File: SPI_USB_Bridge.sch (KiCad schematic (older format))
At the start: 31 parts, among them J6 USB A RECEP., Q5 IRLML2502, Q6 IRLML2502, U15 CY7C65634-28LTXC, U9 MAX3421, Y2 12MHz, Y3 12MHz

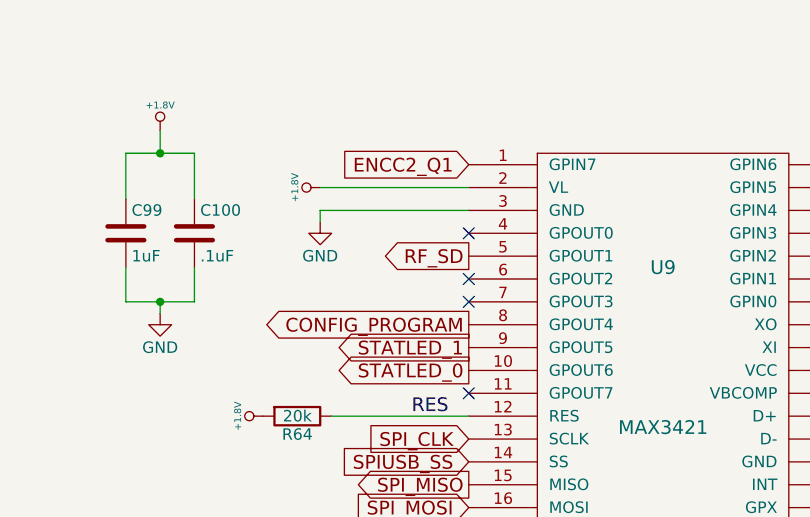
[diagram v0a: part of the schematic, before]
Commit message: encoders and headphone jack have been modified. many unconnections
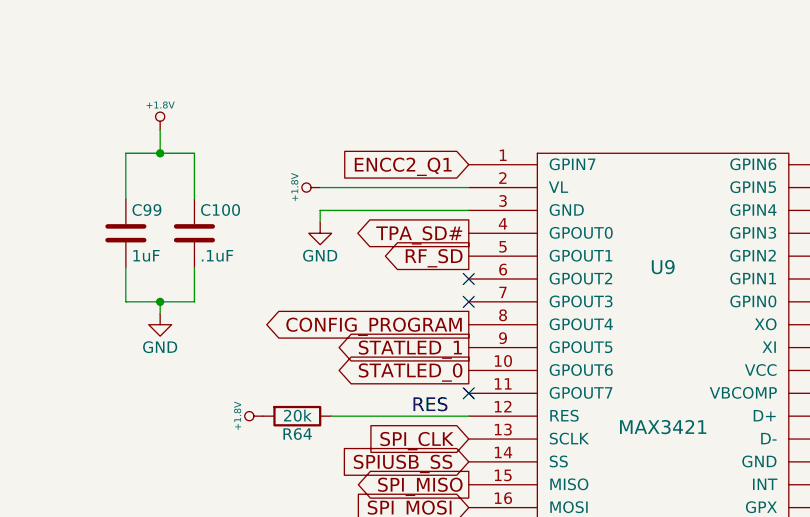
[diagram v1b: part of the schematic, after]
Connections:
- net labels added: TPA_SD#
- no-connect marks 7 -> 6
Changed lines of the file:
@@
 LIBS:DFTCustom
 LIBS:TLV320AIC3104
+LIBS:tpa2010d1
+LIBS:lis2hh12
+LIBS:Ghost
+LIBS:asflmb
+LIBS:er-con06hb-1
+LIBS:jack_trs_4pins
 EELAYER 25 0
 EELAYER END
@@
 $EndComp
 $Comp
-L +1.8V #PWR0168
+L +1.8V #PWR0169
 U 1 1 5862C5D3
 P 1850 1550
-F 0 "#PWR0168" H 1850 1690 20  0001 C CNN
+F 0 "#PWR0169" H 1850 1690 20  0001 C CNN
 F 1 "+1.8V" H 1850 1660 30  0000 C CNN
 F 2 "" H 1850 1550 60  0001 C CNN
@@
 $EndComp
 $Comp
-L GND #PWR0169
+L GND #PWR0170
 U 1 1 5862C61D
 P 1850 2350
-F 0 "#PWR0169" H 1850 2100 50  0001 C CNN
+F 0 "#PWR0170" H 1850 2100 50  0001 C CNN
 F 1 "GND" H 1850 2200 50  0000 C CNN
 F 2 "" H 1850 2350 50  0000 C CNN
@@
 $EndComp
 $Comp
-L GND #PWR0170
+L GND #PWR0171
 U 1 1 5862C682
 P 5650 3350
-F 0 "#PWR0170" H 5650 3100 50  0001 C CNN
+F 0 "#PWR0171" H 5650 3100 50  0001 C CNN
 F 1 "GND" H 5650 3200 50  0000 C CNN
 F 2 "" H 5650 3350 50  0000 C CNN
@@
 SPIUSB_GPX
 $Comp
-L GND #PWR0171
+L GND #PWR0172
 U 1 1 5862D1A5
 P 9050 4750
-F 0 "#PWR0171" H 9050 4500 50  0001 C CNN
+F 0 "#PWR0172" H 9050 4500 50  0001 C CNN
 F 1 "GND" H 9050 4600 50  0000 C CNN
 F 2 "" H 9050 4750 50  0000 C CNN
@@
 $EndComp
 $Comp
-L GND #PWR0172
+L GND #PWR0173
 U 1 1 5862D52A
 P 6750 3200
-F 0 "#PWR0172" H 6750 2950 50  0001 C CNN
+F 0 "#PWR0173" H 6750 2950 50  0001 C CNN
 F 1 "GND" H 6750 3050 50  0000 C CNN
 F 2 "" H 6750 3200 50  0000 C CNN
@@
 $EndComp
 $Comp
-L GND #PWR0173
+L GND #PWR0174
 U 1 1 5862DAA7
 P 6250 1950
-F 0 "#PWR0173" H 6250 1700 50  0001 C CNN
+F 0 "#PWR0174" H 6250 1700 50  0001 C CNN
 F 1 "GND" H 6250 1800 50  0000 C CNN
 F 2 "" H 6250 1950 50  0000 C CNN
@@
 $EndComp
 $Comp
-L +5V #PWR0174
+L +5V #PWR0175
 U 1 1 5862DFFF
 P 7900 1250
-F 0 "#PWR0174" H 7900 1100 50  0001 C CNN
+F 0 "#PWR0175" H 7900 1100 50  0001 C CNN
 F 1 "+5V" H 7900 1390 50  0000 C CNN
 F 2 "" H 7900 1250 50  0000 C CNN
@@
 $EndComp
 $Comp
-L GND #PWR0175
+L GND #PWR0176
 U 1 1 5862E157
 P 8000 1800
-F 0 "#PWR0175" H 8000 1550 50  0001 C CNN
+F 0 "#PWR0176" H 8000 1550 50  0001 C CNN
 F 1 "GND" H 8000 1650 50  0000 C CNN
 F 2 "" H 8000 1800 50  0000 C CNN
@@
 	9200 1650 9200 1750
 $Comp
-L +5V #PWR0176
+L +5V #PWR0177
 U 1 1 5862E815
 P 9200 2150
-F 0 "#PWR0176" H 9200 2000 50  0001 C CNN
+F 0 "#PWR0177" H 9200 2000 50  0001 C CNN
 F 1 "+5V" H 9200 2290 50  0000 C CNN
 F 2 "" H 9200 2150 50  0000 C CNN
@@
 $EndComp
 $Comp
-L GND #PWR0177
+L GND #PWR0178
 U 1 1 586FEB40
 P 2050 7300
-F 0 "#PWR0177" H 2050 7050 50  0001 C CNN
+F 0 "#PWR0178" H 2050 7050 50  0001 C CNN
 F 1 "GND" H 2050 7150 50  0000 C CNN
 F 2 "" H 2050 7300 50  0000 C CNN
@@
 $EndComp
 $Comp
-L GND #PWR0178
+L GND #PWR0179
 U 1 1 586FEDFD
 P 2050 5500
-F 0 "#PWR0178" H 2050 5250 50  0001 C CNN
+F 0 "#PWR0179" H 2050 5250 50  0001 C CNN
 F 1 "GND" H 2050 5350 50  0000 C CNN
 F 2 "" H 2050 5500 50  0000 C CNN
@@
 	2050 6350 2050 6250
 $Comp
-L +5V #PWR0179
+L +5V #PWR0180
 U 1 1 58700335
 P 2050 5950
-F 0 "#PWR0179" H 2050 5800 50  0001 C CNN
+F 0 "#PWR0180" H 2050 5800 50  0001 C CNN
 F 1 "+5V" H 2050 6090 50  0000 C CNN
 F 2 "" H 2050 5950 50  0000 C CNN
@@
 	2050 5950 2050 6050
 $Comp
-L +5V #PWR0180
+L +5V #PWR0181
 U 1 1 58700402
 P 2050 4200
-F 0 "#PWR0180" H 2050 4050 50  0001 C CNN
+F 0 "#PWR0181" H 2050 4050 50  0001 C CNN
 F 1 "+5V" H 2050 4340 50  0000 C CNN
 F 2 "" H 2050 4200 50  0000 C CNN
@@
 	9050 4600 9900 4600
 $Comp
-L +3.3V #PWR0181
+L +3.3V #PWR0182
 U 1 1 58742C2F
 P 6950 2600
-F 0 "#PWR0181" H 6950 2450 50  0001 C CNN
+F 0 "#PWR0182" H 6950 2450 50  0001 C CNN
 F 1 "+3.3V" H 6950 2740 50  0000 C CNN
 F 2 "" H 6950 2600 50  0000 C CNN
@@
 	3200 2800 2600 2800
 $Comp
-L +1.8V #PWR0182
+L +1.8V #PWR0183
 U 1 1 58830992
 P 2300 2800
-F 0 "#PWR0182" H 2300 2940 20  0001 C CNN
+F 0 "#PWR0183" H 2300 2940 20  0001 C CNN
 F 1 "+1.8V" H 2300 2910 30  0000 C CNN
 F 2 "" H 2300 2800 60  0001 C CNN
@@
 $EndComp
 $Comp
-L GND #PWR0183
+L GND #PWR0184
 U 1 1 58830D05
 P 2550 1950
-F 0 "#PWR0183" H 2550 1700 50  0001 C CNN
+F 0 "#PWR0184" H 2550 1700 50  0001 C CNN
 F 1 "GND" H 2550 1800 50  0000 C CNN
 F 2 "" H 2550 1950 50  0000 C CNN
@@
 	1700 1650 2000 1650
 $Comp
-L +1.8V #PWR0184
+L +1.8V #PWR0185
 U 1 1 58830E48
 P 2550 1800
-F 0 "#PWR0184" H 2550 1940 20  0001 C CNN
+F 0 "#PWR0185" H 2550 1940 20  0001 C CNN
 F 1 "+1.8V" H 2550 1910 30  0000 C CNN
 F 2 "" H 2550 1800 60  0001 C CNN
@@
 $EndComp
 $Comp
-L GND #PWR0185
+L GND #PWR0186
 U 1 1 5883B9EA
 P 9750 5150
-F 0 "#PWR0185" H 9750 4900 50  0001 C CNN
+F 0 "#PWR0186" H 9750 4900 50  0001 C CNN
 F 1 "GND" H 9750 5000 50  0000 C CNN
 F 2 "" H 9750 5150 50  0000 C CNN
@@
 SPIUSB2_D_N
 $Comp
-L GND #PWR0186
+L GND #PWR0187
 U 1 1 5883DB26
 P 7200 6300
-F 0 "#PWR0186" H 7200 6050 50  0001 C CNN
+F 0 "#PWR0187" H 7200 6050 50  0001 C CNN
 F 1 "GND" H 7200 6150 50  0000 C CNN
 F 2 "" H 7200 6300 50  0000 C CNN
@@
 Connection ~ 9200 1650
 $Comp
-L +5V #PWR0187
+L +5V #PWR0188
 U 1 1 5883FEC9
 P 7900 2650
-F 0 "#PWR0187" H 7900 2500 50  0001 C CNN
+F 0 "#PWR0188" H 7900 2500 50  0001 C CNN
 F 1 "+5V" H 7900 2790 50  0000 C CNN
 F 2 "" H 7900 2650 50  0000 C CNN
@@
 $EndComp
 $Comp
-L GND #PWR0188
+L GND #PWR0189
 U 1 1 5883FED5
 P 8000 3200
-F 0 "#PWR0188" H 8000 2950 50  0001 C CNN
+F 0 "#PWR0189" H 8000 2950 50  0001 C CNN
 F 1 "GND" H 8000 3050 50  0000 C CNN
 F 2 "" H 8000 3200 50  0000 C CNN
@@
 	9200 3050 9200 3150
 $Comp
-L +5V #PWR0189
+L +5V #PWR0190
 U 1 1 5883FEE8
 P 9200 3550
-F 0 "#PWR0189" H 9200 3400 50  0001 C CNN
+F 0 "#PWR0190" H 9200 3400 50  0001 C CNN
 F 1 "+5V" H 9200 3690 50  0000 C CNN
 F 2 "" H 9200 3550 50  0000 C CNN
@@
 SPIUSB_FAULT1
 $Comp
-L +3.3V #PWR0190
+L +3.3V #PWR0191
 U 1 1 588455D9
 P 5650 4350
-F 0 "#PWR0190" H 5650 4200 50  0001 C CNN
+F 0 "#PWR0191" H 5650 4200 50  0001 C CNN
 F 1 "+3.3V" H 5650 4490 50  0000 C CNN
 F 2 "" H 5650 4350 50  0000 C CNN
@@
 Connection ~ 4500 5350
 $Comp
-L GND #PWR0191
+L GND #PWR0192
 U 1 1 58847DF3
 P 4500 5750
-F 0 "#PWR0191" H 4500 5500 50  0001 C CNN
+F 0 "#PWR0192" H 4500 5500 50  0001 C CNN
 F 1 "GND" H 4500 5600 50  0000 C CNN
 F 2 "" H 4500 5750 50  0000 C CNN
@@
 	4500 5650 4500 5750
 $Comp
-L GND #PWR0192
+L GND #PWR0193
 U 1 1 58847FC6
 P 4500 4750
-F 0 "#PWR0192" H 4500 4500 50  0001 C CNN
+F 0 "#PWR0193" H 4500 4500 50  0001 C CNN
 F 1 "GND" H 4500 4600 50  0000 C CNN
 F 2 "" H 4500 4750 50  0000 C CNN
@@
 	4900 5400 4900 5500
 $Comp
-L +3.3V #PWR0193
+L +3.3V #PWR0194
 U 1 1 5884A193
 P 4900 6000
-F 0 "#PWR0193" H 4900 5850 50  0001 C CNN
+F 0 "#PWR0194" H 4900 5850 50  0001 C CNN
 F 1 "+3.3V" H 4900 6140 50  0000 C CNN
 F 2 "" H 4900 6000 50  0000 C CNN
@@
 	4900 5800 4900 6000
 $Comp
-L +3.3V #PWR0194
+L +3.3V #PWR0195
 U 1 1 5884ACF4
 P 5700 5500
-F 0 "#PWR0194" H 5700 5350 50  0001 C CNN
+F 0 "#PWR0195" H 5700 5350 50  0001 C CNN
 F 1 "+3.3V" H 5700 5640 50  0000 C CNN
 F 2 "" H 5700 5500 50  0000 C CNN
@@
 	5950 5600 5200 5600
 $Comp
-L GND #PWR0195
+L GND #PWR0196
 U 1 1 5884B679
 P 5200 6000
-F 0 "#PWR0195" H 5200 5750 50  0001 C CNN
+F 0 "#PWR0196" H 5200 5750 50  0001 C CNN
 F 1 "GND" H 5200 5850 50  0000 C CNN
 F 2 "" H 5200 6000 50  0000 C CNN
@@
 $EndComp
 $Comp
-L GND #PWR0196
+L GND #PWR0197
 U 1 1 5884BCCD
 P 5450 6000
-F 0 "#PWR0196" H 5450 5750 50  0001 C CNN
+F 0 "#PWR0197" H 5450 5750 50  0001 C CNN
 F 1 "GND" H 5450 5850 50  0000 C CNN
 F 2 "" H 5450 6000 50  0000 C CNN
@@
 	5450 5700 5950 5700
 $Comp
-L GND #PWR0197
+L GND #PWR0198
 U 1 1 5884CAD1
 P 5650 6000
-F 0 "#PWR0197" H 5650 5750 50  0001 C CNN
+F 0 "#PWR0198" H 5650 5750 50  0001 C CNN
 F 1 "GND" H 5650 5850 50  0000 C CNN
 F 2 "" H 5650 6000 50  0000 C CNN
@@
 NoConn ~ 3200 2200
 NoConn ~ 3200 2300
-NoConn ~ 3200 2000
+Text GLabel 3200 2000 0    60   Output ~ 0
+TPA_SD#
 $EndSCHEMATC

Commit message: screen attached!
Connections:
- net labels removed: RF_SD
- no-connect marks 6 -> 7
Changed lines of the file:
@@
 $Descr A4 11693 8268
 encoding utf-8
-Sheet 13 15
+Sheet 13 14
 Title ""
 Date ""
@@
 $EndComp
 $Comp
-L +1.8V #PWR0169
+L +1.8V #PWR0162
 U 1 1 5862C5D3
 P 1850 1550
-F 0 "#PWR0169" H 1850 1690 20  0001 C CNN
+F 0 "#PWR0162" H 1850 1690 20  0001 C CNN
 F 1 "+1.8V" H 1850 1660 30  0000 C CNN
 F 2 "" H 1850 1550 60  0001 C CNN
@@
 $EndComp
 $Comp
-L GND #PWR0170
+L GND #PWR0163
 U 1 1 5862C61D
 P 1850 2350
-F 0 "#PWR0170" H 1850 2100 50  0001 C CNN
+F 0 "#PWR0163" H 1850 2100 50  0001 C CNN
 F 1 "GND" H 1850 2200 50  0000 C CNN
 F 2 "" H 1850 2350 50  0000 C CNN
@@
 $EndComp
 $Comp
-L GND #PWR0171
+L GND #PWR0164
 U 1 1 5862C682
 P 5650 3350
-F 0 "#PWR0171" H 5650 3100 50  0001 C CNN
+F 0 "#PWR0164" H 5650 3100 50  0001 C CNN
 F 1 "GND" H 5650 3200 50  0000 C CNN
 F 2 "" H 5650 3350 50  0000 C CNN
@@
 SPIUSB_GPX
 $Comp
-L GND #PWR0172
+L GND #PWR0165
 U 1 1 5862D1A5
 P 9050 4750
-F 0 "#PWR0172" H 9050 4500 50  0001 C CNN
+F 0 "#PWR0165" H 9050 4500 50  0001 C CNN
 F 1 "GND" H 9050 4600 50  0000 C CNN
 F 2 "" H 9050 4750 50  0000 C CNN
@@
 $EndComp
 $Comp
-L GND #PWR0173
+L GND #PWR0166
 U 1 1 5862D52A
 P 6750 3200
-F 0 "#PWR0173" H 6750 2950 50  0001 C CNN
+F 0 "#PWR0166" H 6750 2950 50  0001 C CNN
 F 1 "GND" H 6750 3050 50  0000 C CNN
 F 2 "" H 6750 3200 50  0000 C CNN
@@
 $EndComp
 $Comp
-L GND #PWR0174
+L GND #PWR0167
 U 1 1 5862DAA7
 P 6250 1950
-F 0 "#PWR0174" H 6250 1700 50  0001 C CNN
+F 0 "#PWR0167" H 6250 1700 50  0001 C CNN
 F 1 "GND" H 6250 1800 50  0000 C CNN
 F 2 "" H 6250 1950 50  0000 C CNN
@@
 $EndComp
 $Comp
-L +5V #PWR0175
+L +5V #PWR0168
 U 1 1 5862DFFF
 P 7900 1250
-F 0 "#PWR0175" H 7900 1100 50  0001 C CNN
+F 0 "#PWR0168" H 7900 1100 50  0001 C CNN
 F 1 "+5V" H 7900 1390 50  0000 C CNN
 F 2 "" H 7900 1250 50  0000 C CNN
@@
 $EndComp
 $Comp
-L GND #PWR0176
+L GND #PWR0169
 U 1 1 5862E157
 P 8000 1800
-F 0 "#PWR0176" H 8000 1550 50  0001 C CNN
+F 0 "#PWR0169" H 8000 1550 50  0001 C CNN
 F 1 "GND" H 8000 1650 50  0000 C CNN
 F 2 "" H 8000 1800 50  0000 C CNN
@@
 	9200 1650 9200 1750
 $Comp
-L +5V #PWR0177
+L +5V #PWR0170
 U 1 1 5862E815
 P 9200 2150
-F 0 "#PWR0177" H 9200 2000 50  0001 C CNN
+F 0 "#PWR0170" H 9200 2000 50  0001 C CNN
 F 1 "+5V" H 9200 2290 50  0000 C CNN
 F 2 "" H 9200 2150 50  0000 C CNN
@@
 Wire Wire Line
 	1700 2300 2000 2300
-Text GLabel 3200 2100 0    60   Output ~ 0
-RF_SD
 Text GLabel 3200 2400 0    60   Output ~ 0
 CONFIG_PROGRAM
@@
 $EndComp
 $Comp
-L GND #PWR0178
+L GND #PWR0171
 U 1 1 586FEB40
 P 2050 7300
-F 0 "#PWR0178" H 2050 7050 50  0001 C CNN
+F 0 "#PWR0171" H 2050 7050 50  0001 C CNN
 F 1 "GND" H 2050 7150 50  0000 C CNN
 F 2 "" H 2050 7300 50  0000 C CNN
@@
 $EndComp
 $Comp
-L GND #PWR0179
+L GND #PWR0172
 U 1 1 586FEDFD
 P 2050 5500
-F 0 "#PWR0179" H 2050 5250 50  0001 C CNN
+F 0 "#PWR0172" H 2050 5250 50  0001 C CNN
 F 1 "GND" H 2050 5350 50  0000 C CNN
 F 2 "" H 2050 5500 50  0000 C CNN
@@
 	2050 6350 2050 6250
 $Comp
-L +5V #PWR0180
+L +5V #PWR0173
 U 1 1 58700335
 P 2050 5950
-F 0 "#PWR0180" H 2050 5800 50  0001 C CNN
+F 0 "#PWR0173" H 2050 5800 50  0001 C CNN
 F 1 "+5V" H 2050 6090 50  0000 C CNN
 F 2 "" H 2050 5950 50  0000 C CNN
@@
 	2050 5950 2050 6050
 $Comp
-L +5V #PWR0181
+L +5V #PWR0174
 U 1 1 58700402
 P 2050 4200
-F 0 "#PWR0181" H 2050 4050 50  0001 C CNN
+F 0 "#PWR0174" H 2050 4050 50  0001 C CNN
 F 1 "+5V" H 2050 4340 50  0000 C CNN
 F 2 "" H 2050 4200 50  0000 C CNN
@@
 	9050 4600 9900 4600
 $Comp
-L +3.3V #PWR0182
+L +3.3V #PWR0175
 U 1 1 58742C2F
 P 6950 2600
-F 0 "#PWR0182" H 6950 2450 50  0001 C CNN
+F 0 "#PWR0175" H 6950 2450 50  0001 C CNN
 F 1 "+3.3V" H 6950 2740 50  0000 C CNN
 F 2 "" H 6950 2600 50  0000 C CNN
@@
 	3200 2800 2600 2800
 $Comp
-L +1.8V #PWR0183
+L +1.8V #PWR0176
 U 1 1 58830992
 P 2300 2800
-F 0 "#PWR0183" H 2300 2940 20  0001 C CNN
+F 0 "#PWR0176" H 2300 2940 20  0001 C CNN
 F 1 "+1.8V" H 2300 2910 30  0000 C CNN
 F 2 "" H 2300 2800 60  0001 C CNN
@@
 $EndComp
 $Comp
-L GND #PWR0184
+L GND #PWR0177
 U 1 1 58830D05
 P 2550 1950
-F 0 "#PWR0184" H 2550 1700 50  0001 C CNN
+F 0 "#PWR0177" H 2550 1700 50  0001 C CNN
 F 1 "GND" H 2550 1800 50  0000 C CNN
 F 2 "" H 2550 1950 50  0000 C CNN
@@
 	1700 1650 2000 1650
 $Comp
-L +1.8V #PWR0185
+L +1.8V #PWR0178
 U 1 1 58830E48
 P 2550 1800
-F 0 "#PWR0185" H 2550 1940 20  0001 C CNN
+F 0 "#PWR0178" H 2550 1940 20  0001 C CNN
 F 1 "+1.8V" H 2550 1910 30  0000 C CNN
 F 2 "" H 2550 1800 60  0001 C CNN
@@
 $EndComp
 $Comp
-L GND #PWR0186
+L GND #PWR0179
 U 1 1 5883B9EA
 P 9750 5150
-F 0 "#PWR0186" H 9750 4900 50  0001 C CNN
+F 0 "#PWR0179" H 9750 4900 50  0001 C CNN
 F 1 "GND" H 9750 5000 50  0000 C CNN
 F 2 "" H 9750 5150 50  0000 C CNN
@@
 SPIUSB2_D_N
 $Comp
-L GND #PWR0187
+L GND #PWR0180
 U 1 1 5883DB26
 P 7200 6300
-F 0 "#PWR0187" H 7200 6050 50  0001 C CNN
+F 0 "#PWR0180" H 7200 6050 50  0001 C CNN
 F 1 "GND" H 7200 6150 50  0000 C CNN
 F 2 "" H 7200 6300 50  0000 C CNN
@@
 Connection ~ 9200 1650
 $Comp
-L +5V #PWR0188
+L +5V #PWR0181
 U 1 1 5883FEC9
 P 7900 2650
-F 0 "#PWR0188" H 7900 2500 50  0001 C CNN
+F 0 "#PWR0181" H 7900 2500 50  0001 C CNN
 F 1 "+5V" H 7900 2790 50  0000 C CNN
 F 2 "" H 7900 2650 50  0000 C CNN
@@
 $EndComp
 $Comp
-L GND #PWR0189
+L GND #PWR0182
 U 1 1 5883FED5
 P 8000 3200
-F 0 "#PWR0189" H 8000 2950 50  0001 C CNN
+F 0 "#PWR0182" H 8000 2950 50  0001 C CNN
 F 1 "GND" H 8000 3050 50  0000 C CNN
 F 2 "" H 8000 3200 50  0000 C CNN
@@
 	9200 3050 9200 3150
 $Comp
-L +5V #PWR0190
+L +5V #PWR0183
 U 1 1 5883FEE8
 P 9200 3550
-F 0 "#PWR0190" H 9200 3400 50  0001 C CNN
+F 0 "#PWR0183" H 9200 3400 50  0001 C CNN
 F 1 "+5V" H 9200 3690 50  0000 C CNN
 F 2 "" H 9200 3550 50  0000 C CNN
@@
 SPIUSB_FAULT1
 $Comp
-L +3.3V #PWR0191
+L +3.3V #PWR0184
 U 1 1 588455D9
 P 5650 4350
-F 0 "#PWR0191" H 5650 4200 50  0001 C CNN
+F 0 "#PWR0184" H 5650 4200 50  0001 C CNN
 F 1 "+3.3V" H 5650 4490 50  0000 C CNN
 F 2 "" H 5650 4350 50  0000 C CNN
@@
 Connection ~ 4500 5350
 $Comp
-L GND #PWR0192
+L GND #PWR0185
 U 1 1 58847DF3
 P 4500 5750
-F 0 "#PWR0192" H 4500 5500 50  0001 C CNN
+F 0 "#PWR0185" H 4500 5500 50  0001 C CNN
 F 1 "GND" H 4500 5600 50  0000 C CNN
 F 2 "" H 4500 5750 50  0000 C CNN
@@
 	4500 5650 4500 5750
 $Comp
-L GND #PWR0193
+L GND #PWR0186
 U 1 1 58847FC6
 P 4500 4750
-F 0 "#PWR0193" H 4500 4500 50  0001 C CNN
+F 0 "#PWR0186" H 4500 4500 50  0001 C CNN
 F 1 "GND" H 4500 4600 50  0000 C CNN
 F 2 "" H 4500 4750 50  0000 C CNN
@@
 	4900 5400 4900 5500
 $Comp
-L +3.3V #PWR0194
+L +3.3V #PWR0187
 U 1 1 5884A193
 P 4900 6000
-F 0 "#PWR0194" H 4900 5850 50  0001 C CNN
+F 0 "#PWR0187" H 4900 5850 50  0001 C CNN
 F 1 "+3.3V" H 4900 6140 50  0000 C CNN
 F 2 "" H 4900 6000 50  0000 C CNN
@@
 	4900 5800 4900 6000
 $Comp
-L +3.3V #PWR0195
+L +3.3V #PWR0188
 U 1 1 5884ACF4
 P 5700 5500
-F 0 "#PWR0195" H 5700 5350 50  0001 C CNN
+F 0 "#PWR0188" H 5700 5350 50  0001 C CNN
 F 1 "+3.3V" H 5700 5640 50  0000 C CNN
 F 2 "" H 5700 5500 50  0000 C CNN
@@
 	5950 5600 5200 5600
 $Comp
-L GND #PWR0196
+L GND #PWR0189
 U 1 1 5884B679
 P 5200 6000
-F 0 "#PWR0196" H 5200 5750 50  0001 C CNN
+F 0 "#PWR0189" H 5200 5750 50  0001 C CNN
 F 1 "GND" H 5200 5850 50  0000 C CNN
 F 2 "" H 5200 6000 50  0000 C CNN
@@
 $EndComp
 $Comp
-L GND #PWR0197
+L GND #PWR0190
 U 1 1 5884BCCD
 P 5450 6000
-F 0 "#PWR0197" H 5450 5750 50  0001 C CNN
+F 0 "#PWR0190" H 5450 5750 50  0001 C CNN
 F 1 "GND" H 5450 5850 50  0000 C CNN
 F 2 "" H 5450 6000 50  0000 C CNN
@@
 	5450 5700 5950 5700
 $Comp
-L GND #PWR0198
+L GND #PWR0191
 U 1 1 5884CAD1
 P 5650 6000
-F 0 "#PWR0198" H 5650 5750 50  0001 C CNN
+F 0 "#PWR0191" H 5650 5750 50  0001 C CNN
 F 1 "GND" H 5650 5850 50  0000 C CNN
 F 2 "" H 5650 6000 50  0000 C CNN
@@
 Text GLabel 3200 2000 0    60   Output ~ 0
 TPA_SD#
+NoConn ~ 3200 2100
 $EndSCHEMATC

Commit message: using BOMs AWAY to create BOM
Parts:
- C100, C104: MFR (none) -> Murata; MPN (none) -> GRM188R71C104KA01D
- C101, C102, C134, C135: MFR (none) -> Murata; MPN (none) -> GRM1555C1H200JA01D
- C103, C99: MFR (none) -> Murata; MPN (none) -> GRM188R71C105KE15D
- D10, D11: MFR (none) -> Vishay Semiconductors; MPN (none) -> VLMB1300-GS08
- J6: MFR (none) -> ASSMANN WSW components; MPN (none) -> AU-Y1008-2
- NCP1, NCP2: MFR (none) -> ON Semiconductor; MPN (none) -> NCP361SNT1G
- Q5, Q6: MFR (none) -> Infineon Technologies AG; MPN (none) -> IRLML2502TRPBF
- R100, R99: MFR (none) -> Vishay Dale; MPN (none) -> CRCW040210K0FKED
- R101: MFR (none) -> YAGEO Corporation; MPN (none) -> RC0402FR-07649RL
- R102, R64, R67: MFR (none) -> Vishay Dale; MPN (none) -> CRCW060320K0FKEA
- R60, R62: MFR (none) -> Vishay Dale; MPN (none) -> CRCW04021K00FKED
- R61, R63: MFR (none) -> Vishay Dale; MPN (none) -> CRCW0402150RFKED
- R65, R66: MFR (none) -> Vishay Dale; MPN (none) -> CRCW040233R0FKED
- U15: MFR (none) -> Cypress Semiconductor; MPN (none) -> CY7C65634-28LTXCT
- U9: MFR (none) -> Maxim Integrated Products; MPN (none) -> MAX3421EEHJ+T
- Y2, Y3: MFR (none) -> ECS International Inc; MPN (none) -> ECS-120-18-5PX-TR

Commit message: just added NOTE field to BOMS AWAY
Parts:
- C100, C104: SPN (none) -> 490-1532-1-ND; SPR (none) -> Digikey
- C101, C102, C134, C135: SPN (none) -> 490-5930-1-ND; SPR (none) -> Digikey
- C103, C99: SPN (none) -> 490-10734-1-ND; SPR (none) -> Digikey
- J6: SPN (none) -> AU-Y1008-2 - Assmann WSW Components AE11131-ND; SPR (none) -> Digikey
- Y2, Y3: SPN (none) -> XC1289CT-ND; SPR (none) -> Digikey
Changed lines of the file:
@@
 F 4 "ECS International Inc" H 0 0 50 0001 C CNN "MFR"
 F 5 "ECS-120-18-5PX-TR" H 0 0 50 0001 C CNN "MPN"
-F 6 "" H 0 0 50 0001 C CNN "SPR"
-F 7 "" H 0 0 50 0001 C CNN "SPN"
+F 6 "Digikey" H 0 0 50 0001 C CNN "SPR"
+F 7 "XC1289CT-ND" H 0 0 50 0001 C CNN "SPN"
 F 8 "" H 0 0 50 0001 C CNN "SPURL"
 	1    6300 2450
@@
 F 4 "Murata" H 0 0 50 0001 C CNN "MFR"
 F 5 "GRM188R71C105KE15D" H 0 0 50 0001 C CNN "MPN"
-F 6 "" H 0 0 50 0001 C CNN "SPR"
-F 7 "" H 0 0 50 0001 C CNN "SPN"
+F 6 "Digikey" H 0 0 50 0001 C CNN "SPR"
+F 7 "490-10734-1-ND" H 0 0 50 0001 C CNN "SPN"
 F 8 "" H 0 0 50 0001 C CNN "SPURL"
 	1    6600 2950
@@
 F 4 "Murata" H 0 0 50 0001 C CNN "MFR"
 F 5 "GRM188R71C104KA01D" H 0 0 50 0001 C CNN "MPN"
-F 6 "" H 0 0 50 0001 C CNN "SPR"
-F 7 "" H 0 0 50 0001 C CNN "SPN"
+F 6 "Digikey" H 0 0 50 0001 C CNN "SPR"
+F 7 "490-1532-1-ND" H 0 0 50 0001 C CNN "SPN"
 F 8 "" H 0 0 50 0001 C CNN "SPURL"
 	1    6900 2950
@@
 F 4 "Murata" H 0 0 50 0001 C CNN "MFR"
 F 5 "GRM1555C1H200JA01D" H 0 0 50 0001 C CNN "MPN"
-F 6 "" H 0 0 50 0001 C CNN "SPR"
-F 7 "" H 0 0 50 0001 C CNN "SPN"
+F 6 "Digikey" H 0 0 50 0001 C CNN "SPR"
+F 7 "490-5930-1-ND" H 0 0 50 0001 C CNN "SPN"
 F 8 "" H 0 0 50 0001 C CNN "SPURL"
 	1    6450 2150
@@
 F 4 "Murata" H 0 0 50 0001 C CNN "MFR"
 F 5 "GRM1555C1H200JA01D" H 0 0 50 0001 C CNN "MPN"
-F 6 "" H 0 0 50 0001 C CNN "SPR"
-F 7 "" H 0 0 50 0001 C CNN "SPN"
+F 6 "Digikey" H 0 0 50 0001 C CNN "SPR"
+F 7 "490-5930-1-ND" H 0 0 50 0001 C CNN "SPN"
 F 8 "" H 0 0 50 0001 C CNN "SPURL"
 	1    6650 2150
@@
 F 4 "Murata" H 0 0 50 0001 C CNN "MFR"
 F 5 "GRM188R71C105KE15D" H 0 0 50 0001 C CNN "MPN"
-F 6 "" H 0 0 50 0001 C CNN "SPR"
-F 7 "" H 0 0 50 0001 C CNN "SPN"
+F 6 "Digikey" H 0 0 50 0001 C CNN "SPR"
+F 7 "490-10734-1-ND" H 0 0 50 0001 C CNN "SPN"
 F 8 "" H 0 0 50 0001 C CNN "SPURL"
 	1    1700 2000
@@
 F 4 "Murata" H 0 0 50 0001 C CNN "MFR"
 F 5 "GRM188R71C104KA01D" H 0 0 50 0001 C CNN "MPN"
-F 6 "" H 0 0 50 0001 C CNN "SPR"
-F 7 "" H 0 0 50 0001 C CNN "SPN"
+F 6 "Digikey" H 0 0 50 0001 C CNN "SPR"
+F 7 "490-1532-1-ND" H 0 0 50 0001 C CNN "SPN"
 F 8 "" H 0 0 50 0001 C CNN "SPURL"
 	1    2000 2000
@@
 F 4 "ECS International Inc" H 0 0 50 0001 C CNN "MFR"
 F 5 "ECS-120-18-5PX-TR" H 0 0 50 0001 C CNN "MPN"
-F 6 "" H 0 0 50 0001 C CNN "SPR"
-F 7 "" H 0 0 50 0001 C CNN "SPN"
+F 6 "Digikey" H 0 0 50 0001 C CNN "SPR"
+F 7 "XC1289CT-ND" H 0 0 50 0001 C CNN "SPN"
 F 8 "" H 0 0 50 0001 C CNN "SPURL"
 	1    4400 5250
@@
 F 4 "Murata" H 0 0 50 0001 C CNN "MFR"
 F 5 "GRM1555C1H200JA01D" H 0 0 50 0001 C CNN "MPN"
-F 6 "" H 0 0 50 0001 C CNN "SPR"
-F 7 "" H 0 0 50 0001 C CNN "SPN"
+F 6 "Digikey" H 0 0 50 0001 C CNN "SPR"
+F 7 "490-5930-1-ND" H 0 0 50 0001 C CNN "SPN"
 F 8 "" H 0 0 50 0001 C CNN "SPURL"
 	1    4500 4950
@@
 F 4 "Murata" H 0 0 50 0001 C CNN "MFR"
 F 5 "GRM1555C1H200JA01D" H 0 0 50 0001 C CNN "MPN"
-F 6 "" H 0 0 50 0001 C CNN "SPR"
-F 7 "" H 0 0 50 0001 C CNN "SPN"
+F 6 "Digikey" H 0 0 50 0001 C CNN "SPR"
+F 7 "490-5930-1-ND" H 0 0 50 0001 C CNN "SPN"
 F 8 "" H 0 0 50 0001 C CNN "SPURL"
 	1    4500 5550
@@
 F 4 "ASSMANN WSW components" H 0 0 50 0001 C CNN "MFR"
 F 5 "AU-Y1008-2" H 0 0 50 0001 C CNN "MPN"
-F 6 "" H 0 0 50 0001 C CNN "SPR"
-F 7 "" H 0 0 50 0001 C CNN "SPN"
+F 6 "Digikey" H 0 0 50 0001 C CNN "SPR"
+F 7 "AU-Y1008-2 - Assmann WSW Components AE11131-ND" H 0 0 50 0001 C CNN "SPN"
 F 8 "" H 0 0 50 0001 C CNN "SPURL"
 	1    10250 4650
